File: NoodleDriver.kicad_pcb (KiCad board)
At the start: 2 copper layers, 36 x 70 mm, 46 parts, among them J1 Conn_01x04, J2 Conn_01x04, J3 Conn_01x02, J4 Conn_01x02_Socket, J5 USB_C_Receptacle_USB2.0_16P, J6 Conn_01x04, J7 Conn_01x04, J8 Conn_01x08, Q1 JSM2302, SW1 On/Off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

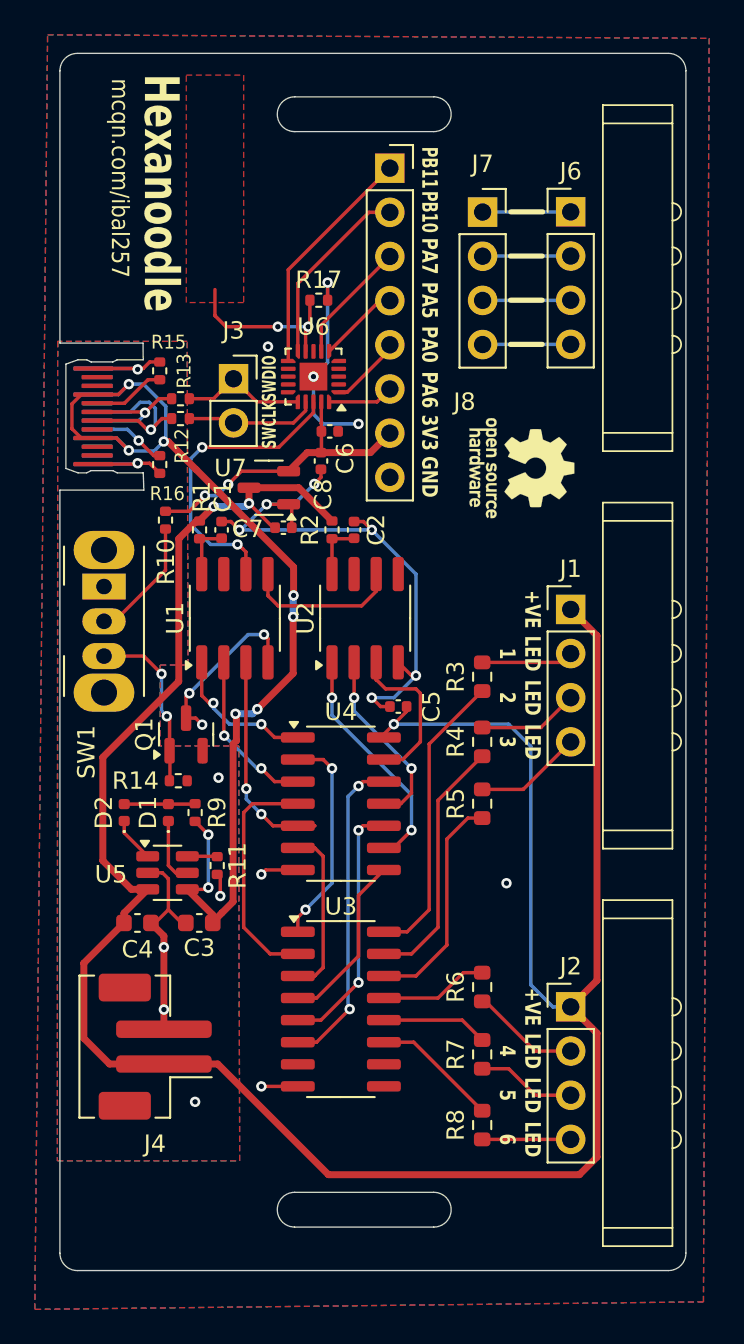
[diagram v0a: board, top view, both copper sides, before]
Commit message: Fix footprint bugs (and remove WS2811 interfaces).  Part of #5
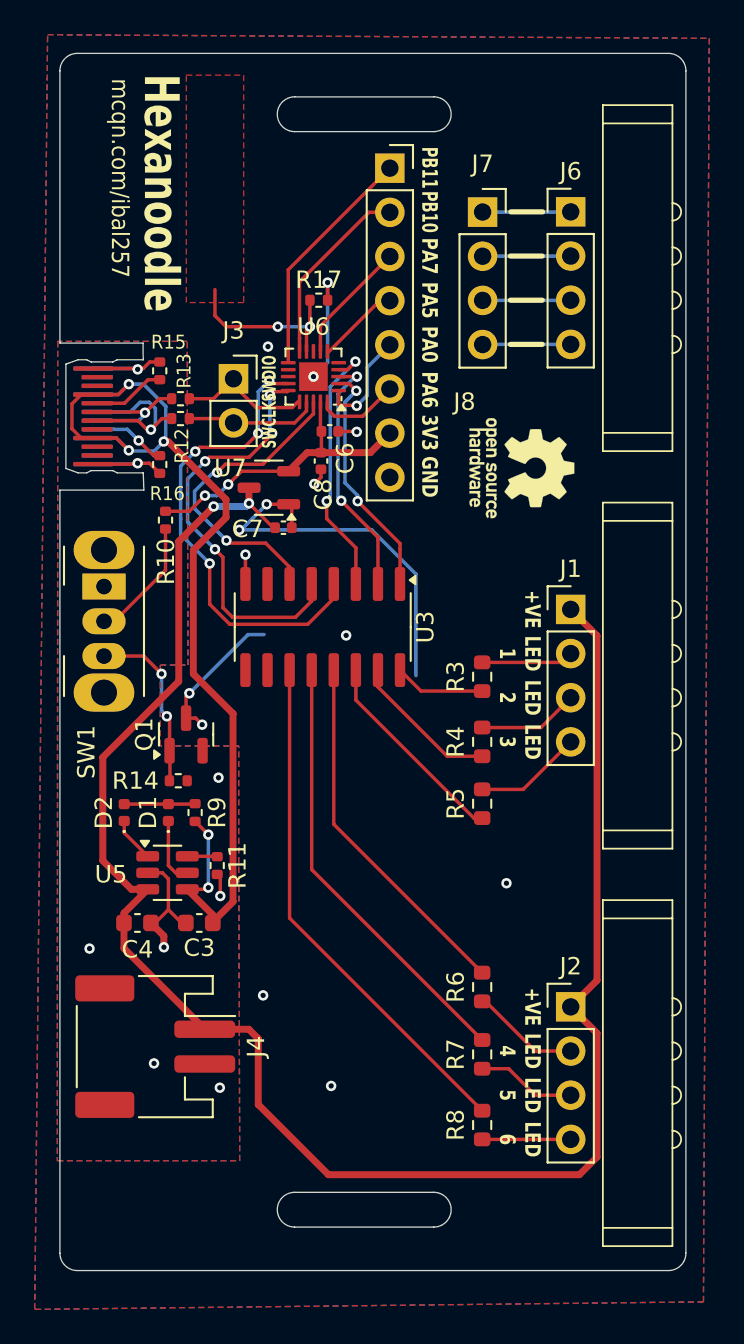
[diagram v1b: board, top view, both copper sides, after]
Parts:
- removed C1, C2: 1uF, Capacitor_SMD:C_0402_1005Metric
- removed C5: 0.1uF, Capacitor_SMD:C_0402_1005Metric
- removed R1, R2: 150R, Resistor_SMD:R_0402_1005Metric
- removed U1, U2: WS2811, Package_SO:SOP-8_3.76x4.96mm_P1.27mm
- removed U4: 74HC04, Package_SO:SOIC-14_3.9x8.7mm_P1.27mm
- J4: footprint Connector_JST:JST_PH_B2B-PH-SM4-TB_1x02-1MP_P2.00mm_Vertical -> Connector_JST:JST_PH_S2B-PH-SM4-TB_1x02-1MP_P2.00mm_Horizontal
- U6: footprint Package_DFN_QFN:QFN-20-1EP_3x3mm_P0.45mm_EP1.6x1.6mm -> Package_DFN_QFN:QFN-20-1EP_3x3mm_P0.4mm_EP1.65x1.65mm
- moved U3 22.0 mm to (167.6, 63.0), turned to -90 degrees
- turned J4 to -90 degrees
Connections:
- U3 pad 1: Net-(U3-I1) -> PA1
- U3 pad 2: Net-(U3-I2) -> PA2
- U3 pad 3: Net-(U3-I3) -> PA3
- U3 pad 4: Net-(U3-I4) -> PA8
- U3 pad 5: Net-(U3-I5) -> PA9
- U3 pad 6: Net-(U3-I6) -> PA10
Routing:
- net +BATT: track 140.9 -> 103.9 mm, vias 3 -> 2
- net PA8: track 0.00 -> 27.4 mm, vias 0 -> 4
- net PA9: track 0.00 -> 24.4 mm, vias 0 -> 4
- net Net-(U3-O6): track 7.28 -> 29.9 mm
- net GND: track 60.3 -> 40.7 mm, vias 16 -> 14
- net Net-(U3-O5): track 6.13 -> 25.3 mm
- net Net-(U3-I6): track 18.4 -> 0.00 mm, vias 2 -> 0
- net PA3: track 0.00 -> 15.3 mm, vias 0 -> 2
- net Net-(U3-I5): track 14.7 -> 0.00 mm, vias 2 -> 0
- net Net-(U3-O4): track 6.26 -> 20.9 mm
- net PA2: track 0.00 -> 14.4 mm, vias 0 -> 2
- net PA1: track 0.00 -> 13.9 mm, vias 0 -> 2
- net Net-(U3-I2): track 13.7 -> 0.00 mm
- net Net-(U2-OUTR): track 13.6 -> 0.00 mm, vias 2 -> 0
- net Net-(U1-OUTB): track 13.4 -> 0.00 mm, vias 2 -> 0
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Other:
- board text added: "r20251010"
- board text removed: "r20250924"
